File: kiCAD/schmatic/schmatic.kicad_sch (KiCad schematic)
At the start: 35 parts, among them J1 USB_C_Receptacle, J2 Conn_02x03_Counter_Clockwise, SW1 SW_MEC_5G, U1 STM32F401CBUx, U2 MPU-9250, U3 LP5907MFX-3.3, U4 USBLC6-2SC6, U5 XGZP6859D, Y1 16MHz, Y2 Crystal

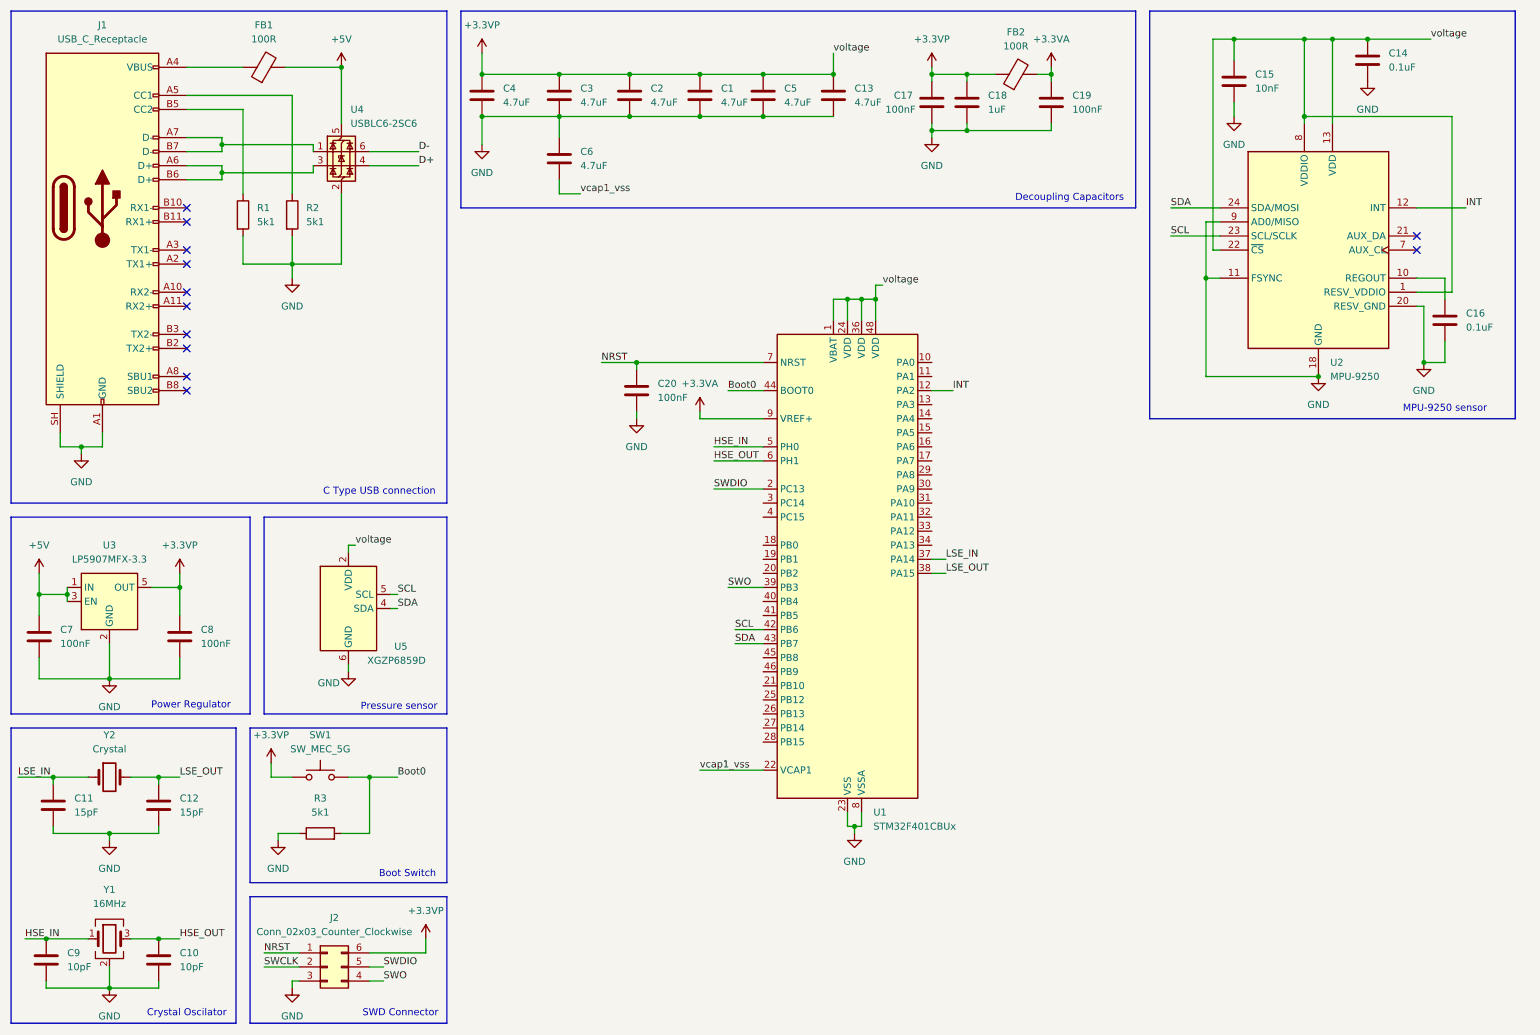
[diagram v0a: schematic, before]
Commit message: feat: ERC fixes and footprint assignment
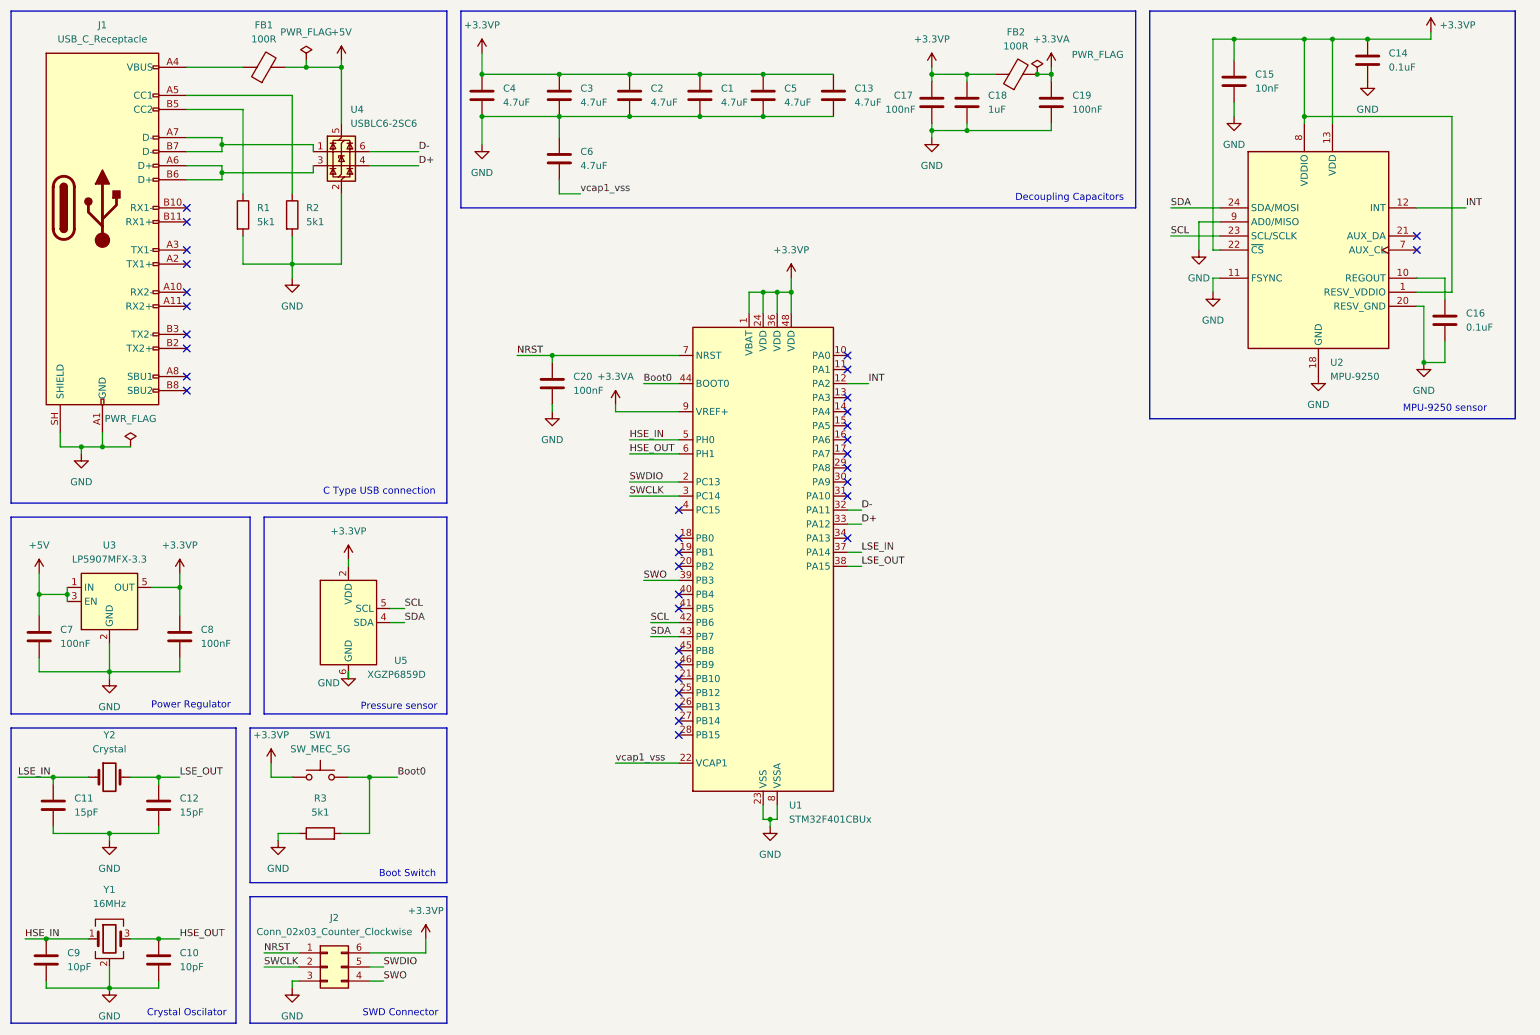
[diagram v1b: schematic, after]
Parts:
- C1, C13, C2, C3, C4, C5, C6: footprint (none) -> Capacitor_SMD:C_0805_2012Metric
- C10, C11, C12, C14, C15, C16, C17, C19, C20, C7, C8, C9: footprint (none) -> Capacitor_SMD:C_0603_1608Metric
- C18: footprint (none) -> Capacitor_SMD:C_0603_1608Metric_Pad1.08x0.95mm_HandSolder
- FB1, FB2: footprint (none) -> Capacitor_SMD:C_0201_0603Metric
- J1: footprint (none) -> Connector_USB:USB_C_Receptacle_HRO_TYPE-C-31-M-12
- J2: footprint (none) -> Connector_PinHeader_2.54mm:PinHeader_1x01_P2.54mm_Horizontal
- R1, R2, R3: footprint (none) -> Resistor_THT:R_Axial_DIN0207_L6.3mm_D2.5mm_P7.62mm_Horizontal
- Y1, Y2: footprint (none) -> Crystal:Crystal_SMD_3225-4Pin_3.2x2.5mm
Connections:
- net D+: now also U1.33 (PA12)
- net D-: now also U1.32 (PA11)
- net SWCLK: now also U1.3 (PC14)
- no-connect marks 12 -> 36
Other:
- company: (none) -> IIITN
- title: (none) -> Flight Computer 3-DOF
- moved on the sheet: C20, U1, U5

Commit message: feat: fixed footprint issue and updated readme
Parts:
- added R4, R5: R, Resistor_THT:R_Axial_DIN0207_L6.3mm_D2.5mm_P7.62mm_Horizontal, symbol Device:R
- J1: footprint Connector_USB:USB_C_Receptacle_HRO_TYPE-C-31-M-12 -> Connector_USB:USB_C_Receptacle_Molex_105450-0101
- J2: footprint Connector_PinHeader_2.54mm:PinHeader_1x01_P2.54mm_Horizontal -> Connector_PinHeader_2.54mm:PinHeader_2x03_P2.54mm_Vertical
- U2: footprint Sensor_Motion:InvenSense_QFN-24_3x3mm_P0.4mm -> Sensor_Motion:InvenSense_QFN-24_4x4mm_P0.5mm_NoMask
- Y2: footprint Crystal:Crystal_SMD_3225-4Pin_3.2x2.5mm -> Crystal:Crystal_SMD_5032-2Pin_5.0x3.2mm
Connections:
- net +3.3VP: now also R4.1, R5.1
- net SCL: now also R5.2
- net SDA: now also R4.2
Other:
- note added: "I2C Pull Up Resistor"
